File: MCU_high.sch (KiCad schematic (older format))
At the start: 85 parts, among them J11 STLinkV2, J12 Nucleo_SWD, J15 Conn_02x03_Odd_Even, J16 Conn_02x03_Odd_Even, SW11 RST, U33 ADS131M06, U34 STM32L431RBTx, Y4 8.192, Y5 8.192, Y6 32.768

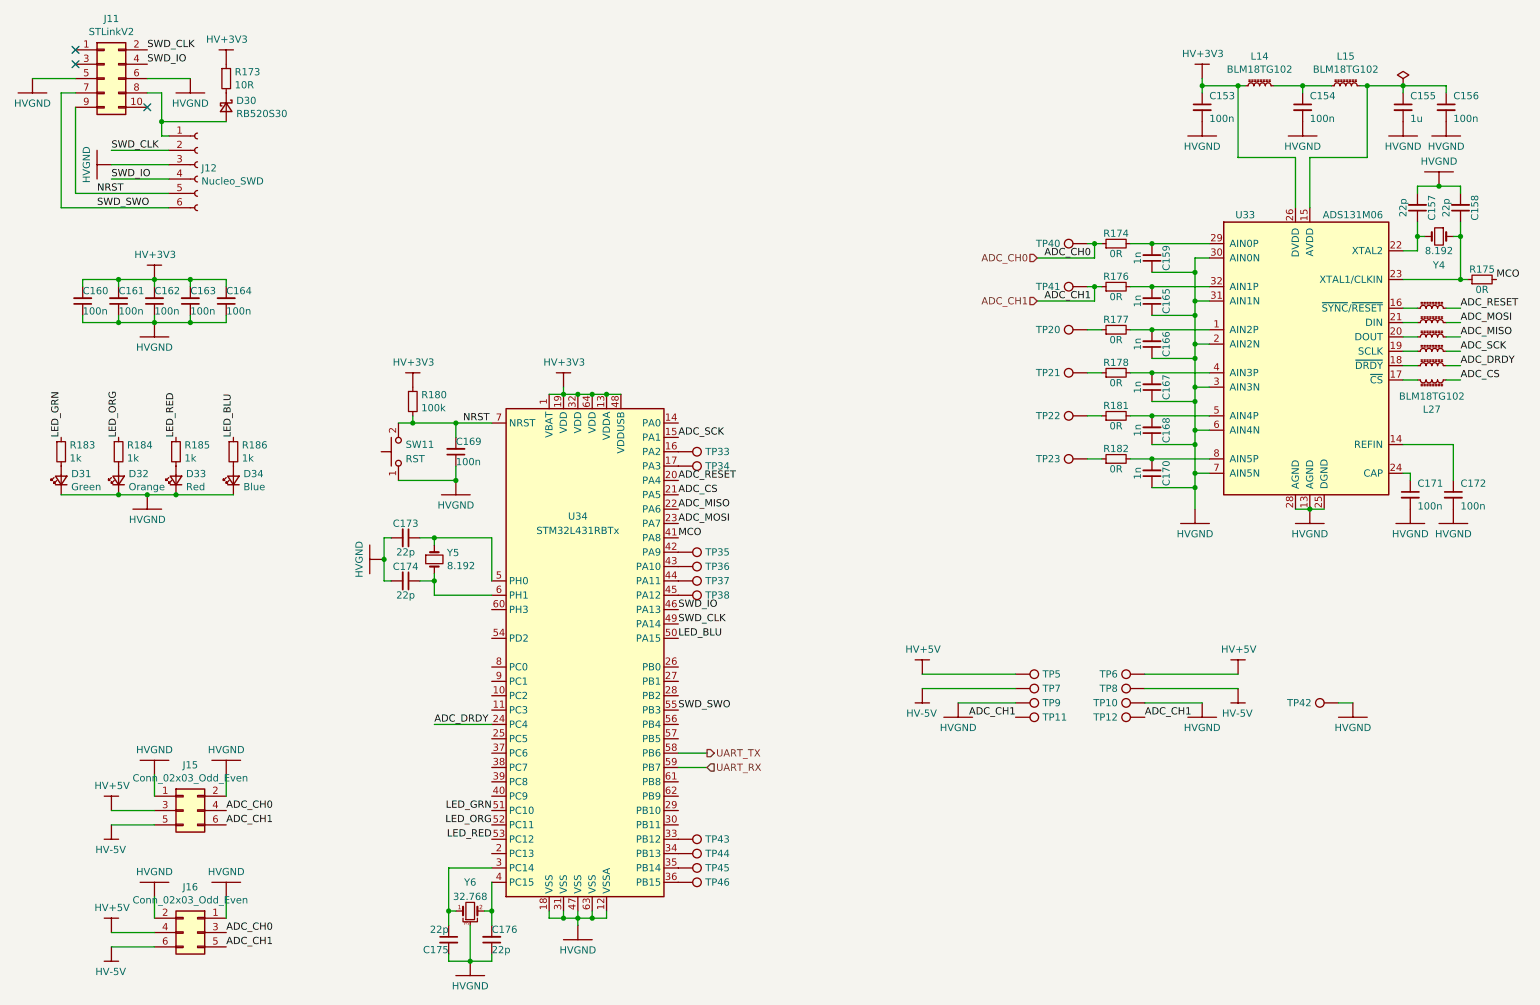
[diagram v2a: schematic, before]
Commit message: - as-built changes - add custom library elements
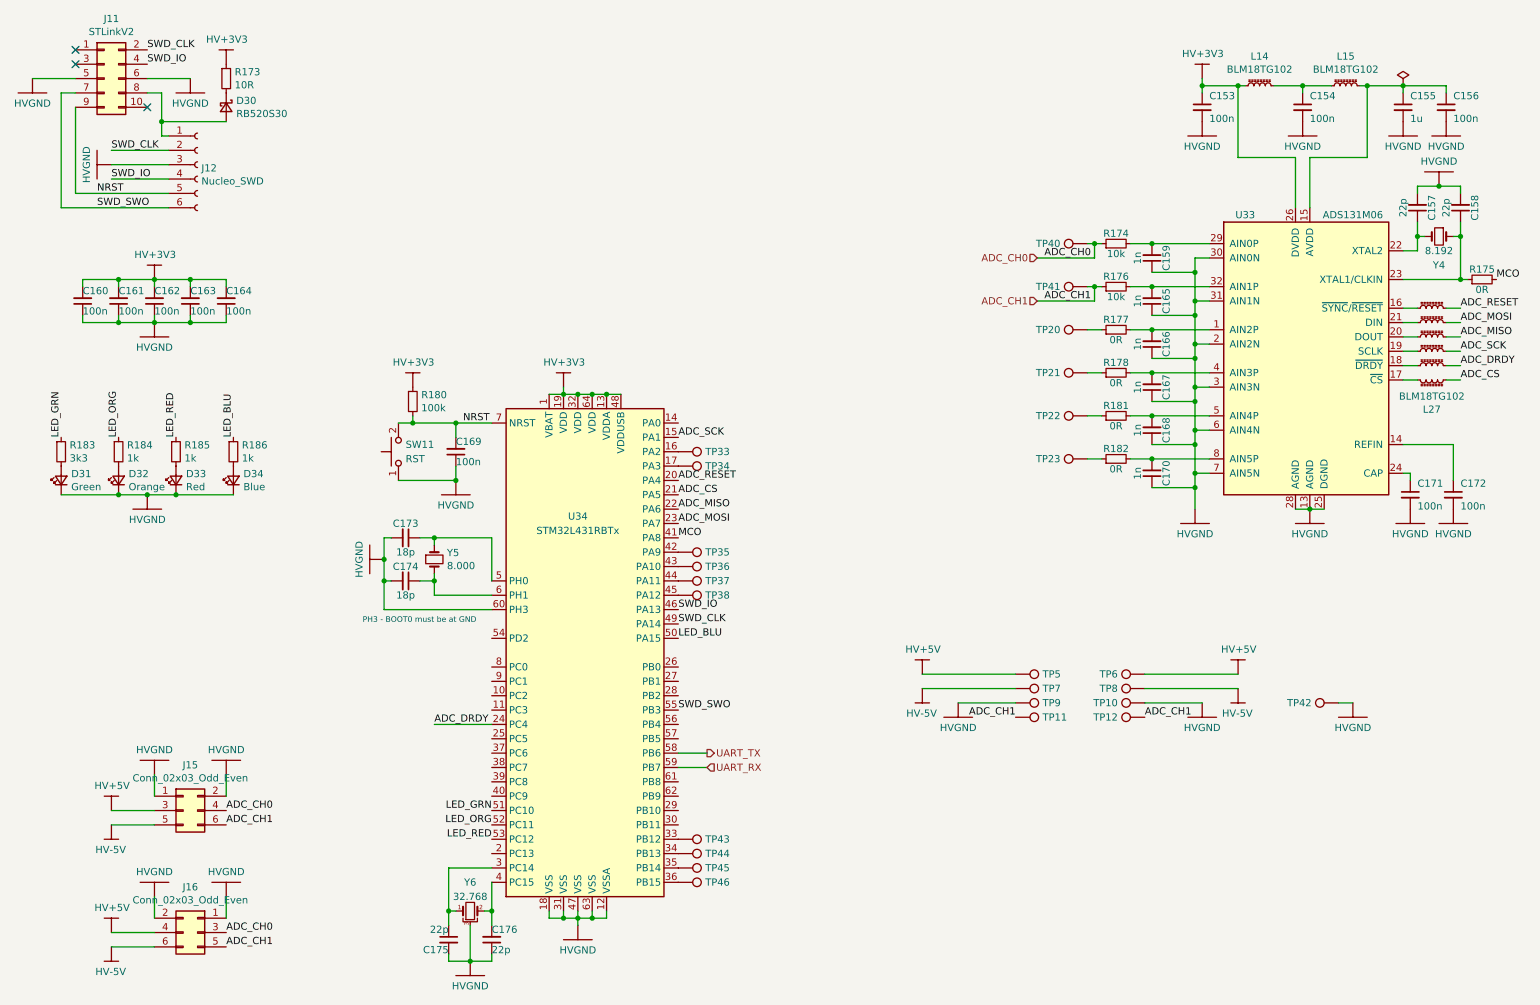
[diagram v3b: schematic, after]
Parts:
- C173, C174: value 22p -> 18p
- R174, R176: value 0R -> 10k
- R183: value 1k -> 3k3
- Y5: value 8.192 -> 8.000
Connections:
- net HVGND: now also U34.60 (PH3)
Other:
- note added: "PH3 - BOOT0 must be at GND"
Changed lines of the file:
@@
 encoding utf-8
 Sheet 9 10
-Title ""
-Date ""
-Rev ""
-Comp ""
+Title "Procesor - katoda"
+Date "2021-01-18"
+Rev "1.0"
+Comp "Łukasz Sitarek"
 Comment1 ""
 Comment2 ""
@@
 AR Path="/5F8337DC/5FA3968D" Ref="Y5"  Part="1"
 F 0 "Y5" V 3454 4538 50  0000 L CNN
-F 1 "8.192" V 3545 4538 50  0000 L CNN
+F 1 "8.000" V 3545 4538 50  0000 L CNN
 F 2 "Crystal:Crystal_HC49-4H_Vertical" H 3500 4450 50  0001 C CNN
 F 3 "~" H 3500 4450 50  0001 C CNN
@@
 AR Path="/5F8337DC/5FA39694" Ref="C173"  Part="1"
 F 0 "C173" V 3200 4300 50  0000 C CNN
-F 1 "22p" V 3400 4300 50  0000 C CNN
+F 1 "18p" V 3400 4300 50  0000 C CNN
 F 2 "Capacitor_SMD:C_0603_1608Metric" H 3300 4300 50  0001 C CNN
 F 3 "~" H 3300 4300 50  0001 C CNN
@@
 AR Path="/5F8337DC/5FA3969B" Ref="C174"  Part="1"
 F 0 "C174" V 3200 4600 50  0000 C CNN
-F 1 "22p" V 3400 4600 50  0000 C CNN
+F 1 "18p" V 3400 4600 50  0000 C CNN
 F 2 "Capacitor_SMD:C_0603_1608Metric" H 3300 4600 50  0001 C CNN
 F 3 "~" H 3300 4600 50  0001 C CNN
@@
 AR Path="/5F8337DC/5FD413EF" Ref="R183"  Part="1"
 F 0 "R183" H 959 3746 50  0000 L CNN
-F 1 "1k" H 959 3655 50  0000 L CNN
+F 1 "3k3" H 959 3655 50  0000 L CNN
 F 2 "Resistor_SMD:R_0603_1608Metric" H 900 3700 50  0001 C CNN
 F 3 "~" H 900 3700 50  0001 C CNN
@@
 AR Path="/5F8337DC/60004820" Ref="R174"  Part="1"
 F 0 "R174" V 8350 2250 50  0000 C BNN
-F 1 "0R" V 8150 2250 50  0000 C TNN
+F 1 "10k" V 8150 2250 50  0000 C TNN
 F 2 "Resistor_SMD:R_0603_1608Metric" V 8180 2250 50  0001 C CNN
 F 3 "~" H 8250 2250 50  0001 C CNN
@@
 AR Path="/5F8337DC/60004835" Ref="R176"  Part="1"
 F 0 "R176" V 8350 2550 50  0000 C BNN
-F 1 "0R" V 8150 2550 50  0000 C TNN
+F 1 "10k" V 8150 2550 50  0000 C TNN
 F 2 "Resistor_SMD:R_0603_1608Metric" V 8180 2550 50  0001 C CNN
 F 3 "~" H 8250 2550 50  0001 C CNN
@@
 Text Label 7550 5550 2    50   ~ 0
 ADC_CH1
+Wire Wire Line
+	3900 4800 3150 4800
+Wire Wire Line
+	3150 4800 3150 4600
+Connection ~ 3150 4600
+Text Notes 3000 4900 0    39   ~ 0
+PH3 - BOOT0 must be at GND
 $EndSCHEMATC
